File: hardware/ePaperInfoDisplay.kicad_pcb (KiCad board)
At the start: 2 copper layers, 93.2 x 22.9 mm, 52 parts, among them J1 Conn_01x02_Pin, J2 USB_C_Receptacle_USB2.0, Q1 Q_NMOS_GSD, Q2 Q_PMOS_GSD, Q3 Q_PMOS_GSD, SW1 SW_Push, SW2 SW_Push, U1 MCP73831-2-OT, U2 MIC5219-3.3YM5, U3 ePD_iTC

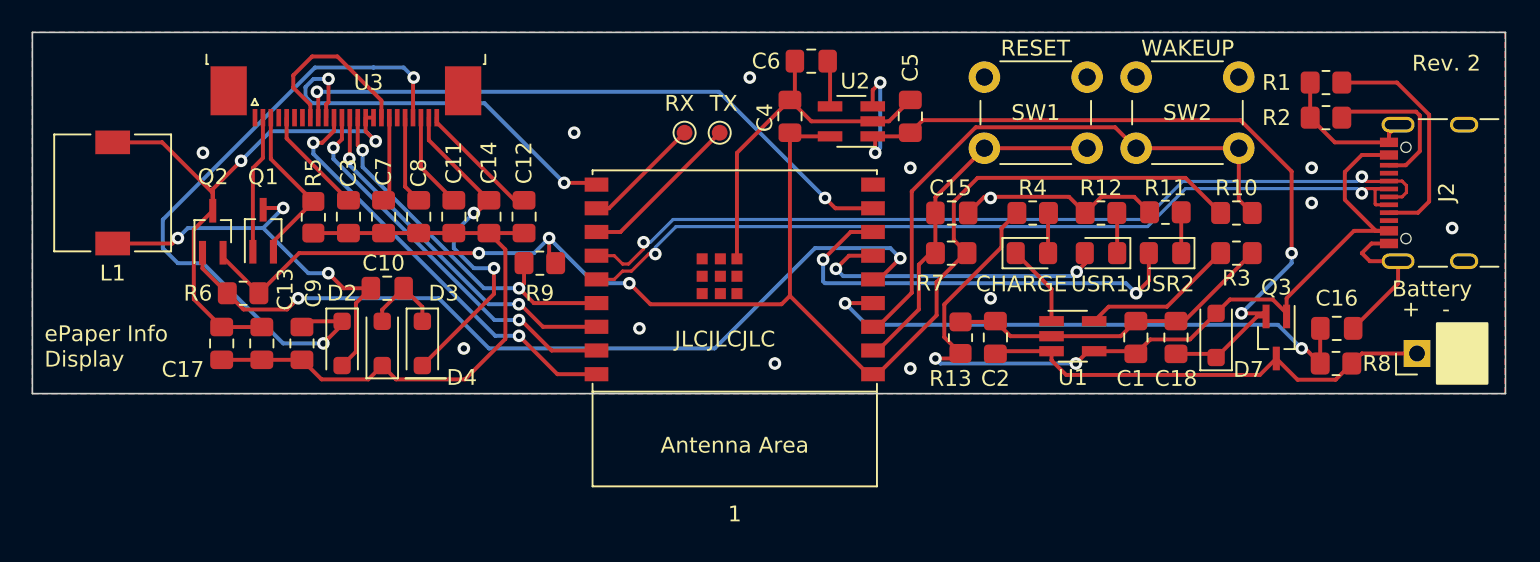
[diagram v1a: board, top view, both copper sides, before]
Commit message: Update hardware to Rev. 3
Fixed all of the known issues:
- Fixed swapped USB DP+/-, USB usable again
- Fixed swapped labels USR1/USR2
- Add resistor divider for VBAT_SENSE to avoid excessive voltage on GPIO pin
- WAKEUP button changed to BOOT (connected to GPIO9)
- VBAT_SENSE moved to GPIO4 which has a usable ADC
- GPIO association of some signals changed to avoid issues strapping pins:
	- LED1 now on GPIO5
	- LED2 now on GPIO6
	- /BUSY now on GPIO7
	- /PWR_EN now on GPIO8
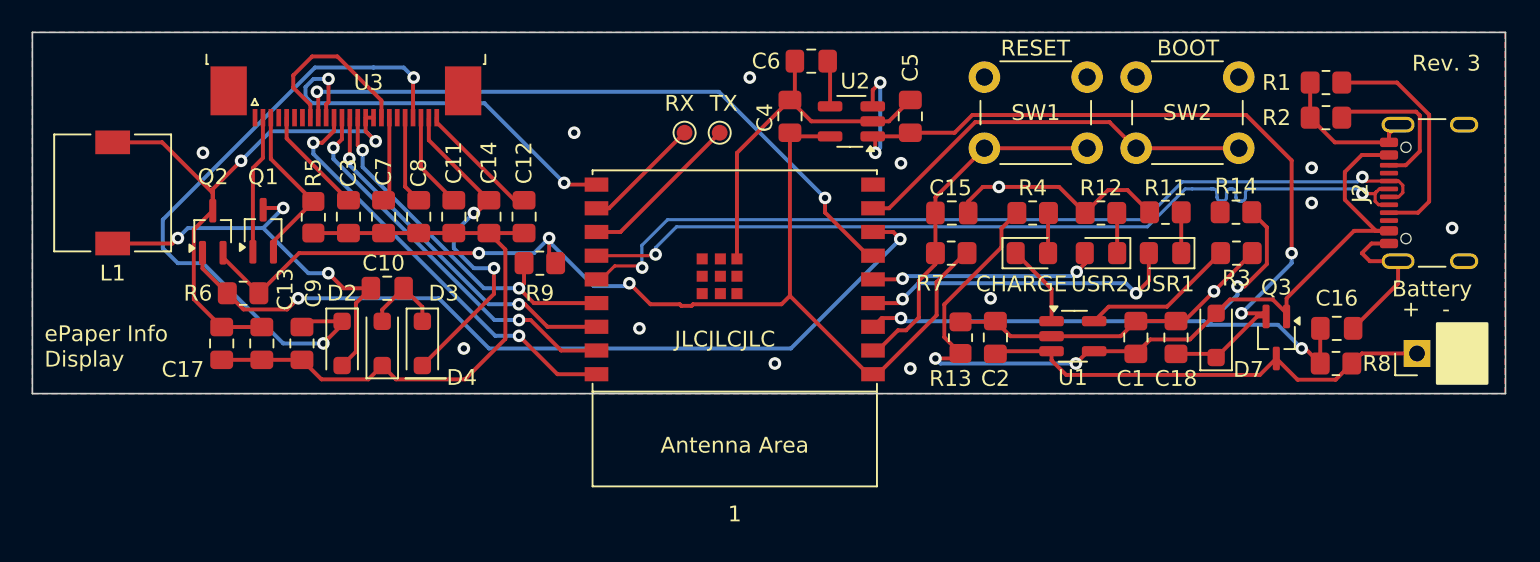
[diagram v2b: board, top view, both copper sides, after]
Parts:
- removed R10: 10K, Resistor_SMD:R_0805_2012Metric_Pad1.20x1.40mm_HandSolder
- added R14: 10K, Resistor_SMD:R_0805_2012Metric_Pad1.20x1.40mm_HandSolder, F.Cu at (189.2, 82.5)
- R4: value 470R -> 1K
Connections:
- 1 pad 13: /USB_D+ -> /USB_D-
- 1 pad 14: /USB_D- -> /USB_D+
- 1 pad 3: /WAKEUP -> /VBAT_SENSE
- 1 pad 4: /VBAT_SENSE -> /LED1
- 1 pad 5: /~{PWR_EN} -> /LED2
- 1 pad 6: /LED2 -> /~{BUSY}
- 1 pad 7: /LED1 -> /~{PWR_EN}
- 1 pad 8: /~{BUSY} -> /BOOT
- SW2 pad 2: /WAKEUP -> /BOOT
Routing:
- net /WAKEUP: track 37.1 -> 0.00 mm
- net /BOOT: track 0.00 -> 26.1 mm
- net +3V3: track 94.9 -> 73.3 mm
- net /LED1: track 28.3 -> 20.3 mm
- net /VBAT_SENSE: track 35.6 -> 41.3 mm, vias 2 -> 3
- net /LED2: track 19.6 -> 14.9 mm
- net /~{BUSY}: track 39.9 -> 41.7 mm
- net GND: track 128.5 -> 129.7 mm, vias 13 -> 14
- net +BATT: track 54.5 -> 55.1 mm
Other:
- board text added: "BOOT"
- board text added: "Rev. 3"
- board text added: "© 2025 Niklas Rother"
- board text removed: "Rev. 2"
- board text removed: "WAKEUP"
- board text removed: "© 2024 Niklas Rother"
